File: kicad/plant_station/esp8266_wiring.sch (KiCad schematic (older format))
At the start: 20 parts, among them J1 Conn_02x08_Odd_Even, J17 GPIO, J8 UART, Q4 DMG2301L, U4 ESP-WROOM-02, U5 TPL5110

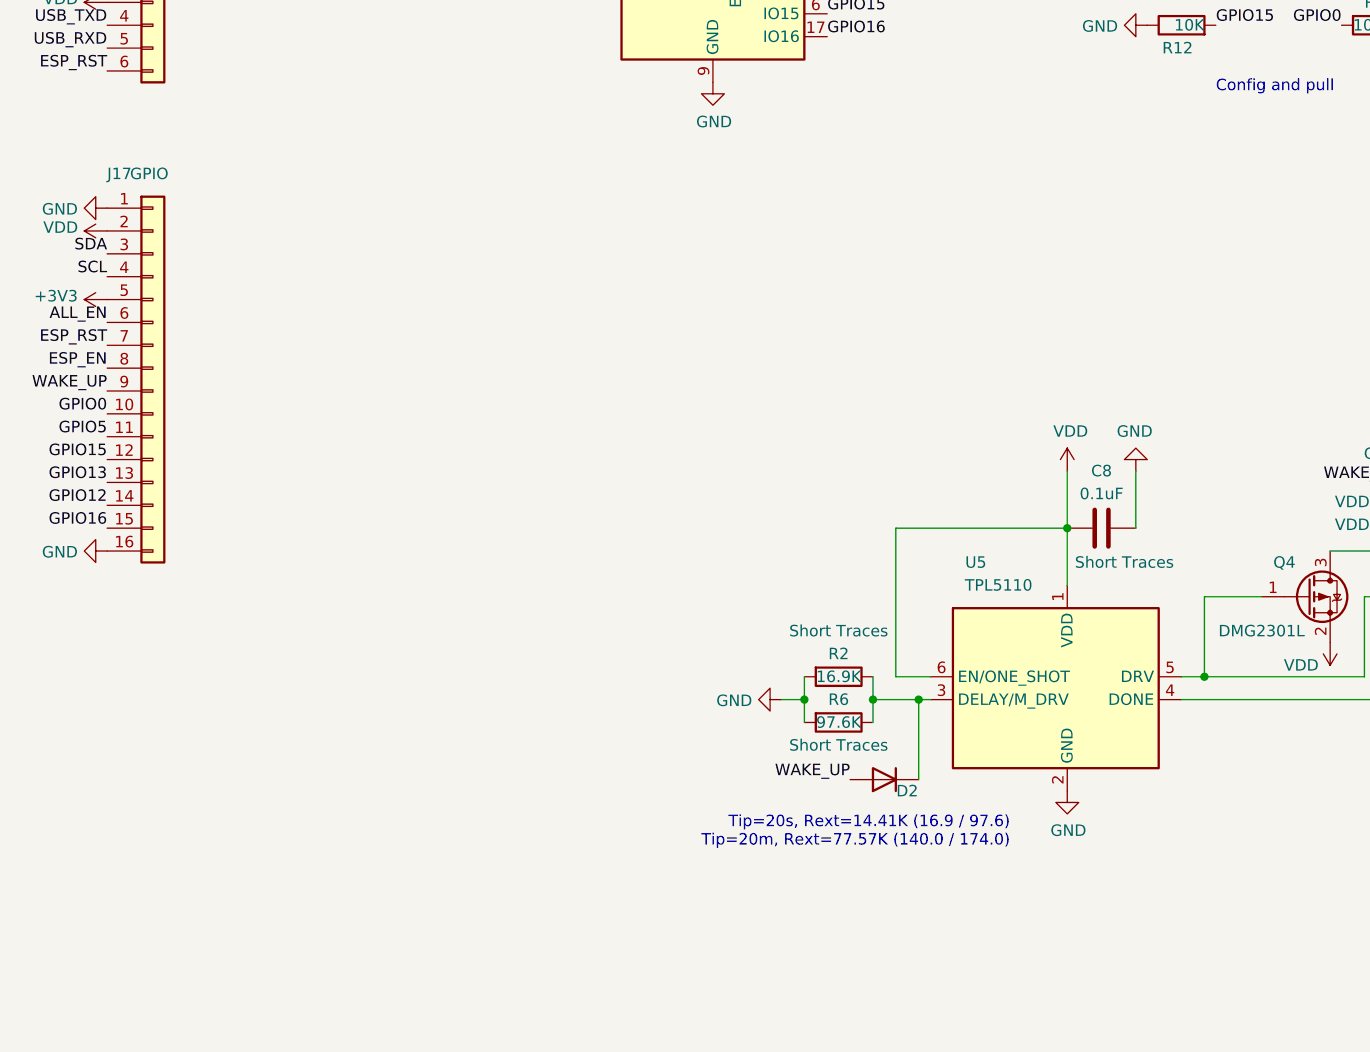
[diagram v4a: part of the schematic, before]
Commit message: Pre-refactoring, diagnostics complete, timer not working properly
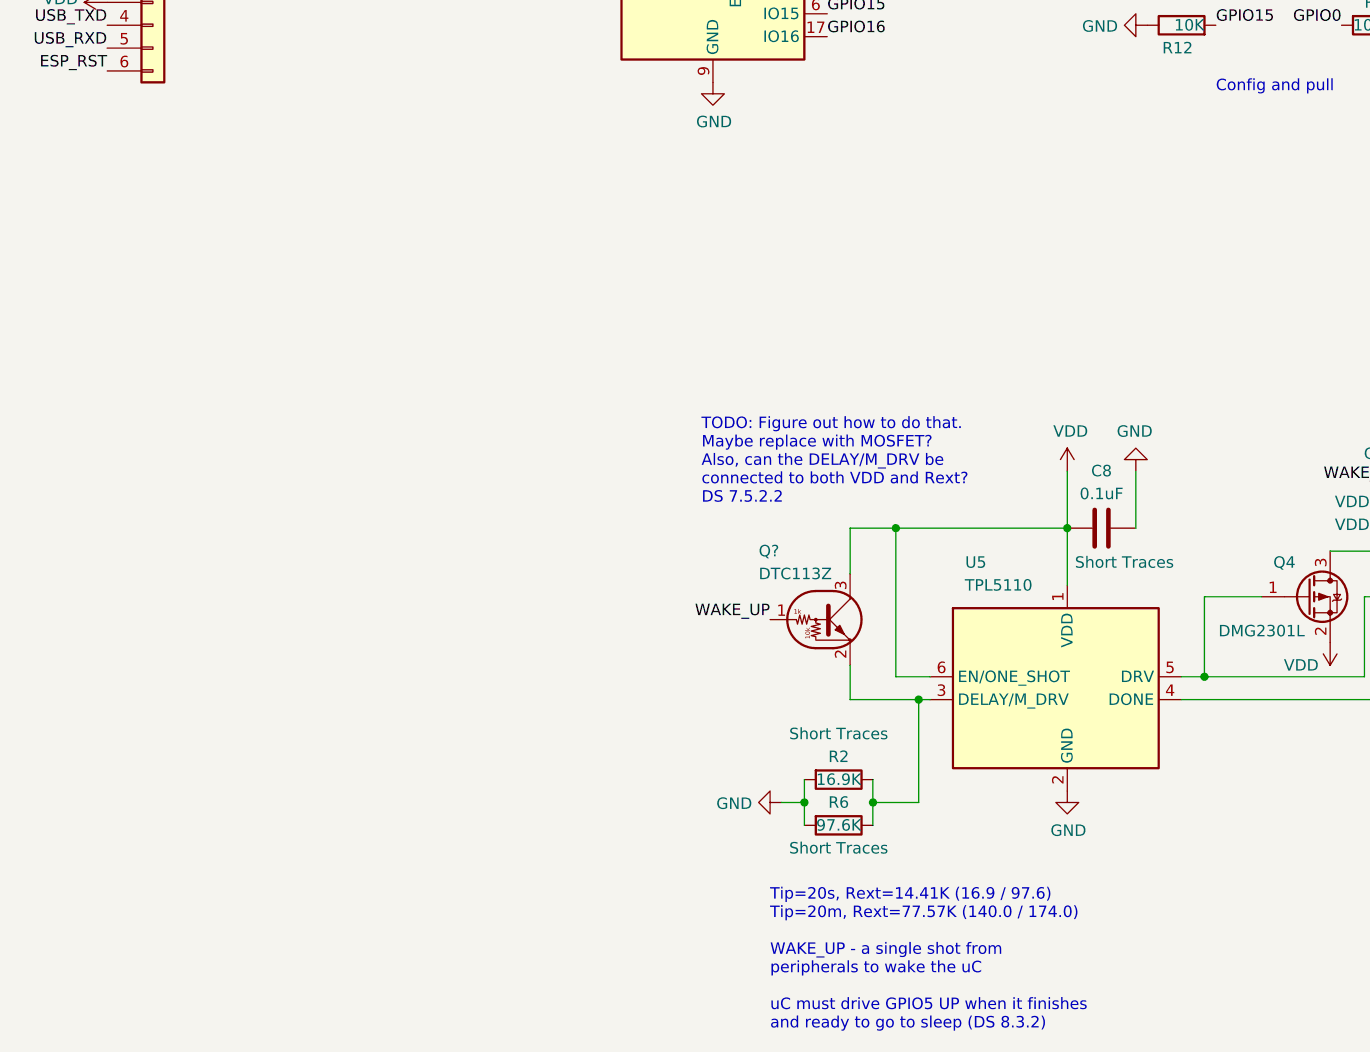
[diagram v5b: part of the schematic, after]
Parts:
- removed D2: LS4148, Parts:MELF_SOD_80_3_BZT55B13GS08, symbol Device:D
- removed J17: GPIO, Connector_PinHeader_2.54mm:PinHeader_1x16_P2.54mm_Vertical, symbol Connector_Generic:Conn_01x16
- added Q?: DTC113Z, symbol Transistor_BJT:DTC113Z
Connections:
- net HOST_WAKE_UP: now also Q?.1 (B)
- net VDD: now also Q?.3 (C)
- net at R2.1, R6.1, U5.3 (DELAY/M_DRV): now also Q?.2 (E)
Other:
- note added: "TODO: Figure out how to do that.\nMaybe replace with MOSFET?\nAlso, can the DELAY/M_DRV be \nconnected to both VDD and Rext? \nDS 7.5.2.2"
- note added: "Tip=20s, Rext=14.41K (16.9 / 97.6)\nTip=20m, Rext=77.57K (140.0 / 174.0)\n\nWAKE_UP - a single shot from \nperipherals to wake the uC\n\nuC must drive GPIO5 UP when it finishes \nand ready to go to sleep (DS 8.3.2)"
- note removed: "Tip=20s, Rext=14.41K (16.9 / 97.6)\nTip=20m, Rext=77.57K (140.0 / 174.0)"
- moved on the sheet: R2, R6
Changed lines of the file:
@@
 	1    0    0    -1
 $EndComp
-Text Label 1900 3900 2    50   ~ 0
-ESP_RST
 $Comp
 L power:GND #PWR049
@@
 L power:GND #PWR031
 U 1 1 5F7FBED9
-P 4850 5450
-F 0 "#PWR031" H 4850 5200 50  0001 C CNN
-F 1 "GND" V 4855 5322 50  0000 R CNN
-F 2 "" H 4850 5450 50  0001 C CNN
-F 3 "" H 4850 5450 50  0001 C CNN
-	1    4850 5450
+P 4850 5900
+F 0 "#PWR031" H 4850 5650 50  0001 C CNN
+F 1 "GND" V 4855 5772 50  0000 R CNN
+F 2 "" H 4850 5900 50  0001 C CNN
+F 3 "" H 4850 5900 50  0001 C CNN
+	1    4850 5900
 	0    1    1    0
 $EndComp
@@
 L Device:R R2
 U 1 1 5F800035
-P 5100 5350
-F 0 "R2" V 5000 5350 50  0000 C CNN
-F 1 "16.9K" V 5100 5350 50  0000 C CNN
-F 2 "Resistor_SMD:R_0805_2012Metric" V 5030 5350 50  0001 C CNN
-F 3 "~" H 5100 5350 50  0001 C CNN
-F 4 "Short Traces" V 4900 5350 50  0000 C CNN "Note"
-	1    5100 5350
-	0    1    1    0
-$EndComp
-Text Label 5150 5800 2    50   ~ 0
+P 5100 5800
+F 0 "R2" V 5000 5800 50  0000 C CNN
+F 1 "16.9K" V 5100 5800 50  0000 C CNN
+F 2 "Resistor_SMD:R_0805_2012Metric" V 5030 5800 50  0001 C CNN
+F 3 "~" H 5100 5800 50  0001 C CNN
+F 4 "Short Traces" V 4900 5800 50  0000 C CNN "Note"
+	1    5100 5800
+	0    1    1    0
+$EndComp
+Text Label 4800 5100 2    50   ~ 0
 WAKE_UP
-$Comp
-L Device:D D2
-U 1 1 5F80D3D3
-P 5300 5800
-F 0 "D2" H 5200 5850 50  0000 C CNN
-F 1 "LS4148" H 5200 5750 50  0001 C CNN
-F 2 "Parts:MELF_SOD_80_3_BZT55B13GS08" H 5300 5800 50  0001 C CNN
-F 3 "~" H 5300 5800 50  0001 C CNN
-	1    5300 5800
-	-1   0    0    1
-$EndComp
-Wire Wire Line
-	5250 5450 5450 5450
-Connection ~ 5450 5450
+Wire Wire Line
+	5250 5900 5450 5900
 Wire Wire Line
 	5450 5450 5500 5450
-Text Notes 5850 6100 2    50   ~ 0
-Tip=20s, Rext=14.41K (16.9 / 97.6)\nTip=20m, Rext=77.57K (140.0 / 174.0)
+Text Notes 4800 6900 0    50   ~ 0
+Tip=20s, Rext=14.41K (16.9 / 97.6)\nTip=20m, Rext=77.57K (140.0 / 174.0)\n\nWAKE_UP - a single shot from \nperipherals to wake the uC\n\nuC must drive GPIO5 UP when it finishes \nand ready to go to sleep (DS 8.3.2)
 $Comp
 L Device:R R6
 U 1 1 5F850A50
-P 5100 5550
-F 0 "R6" V 5000 5550 50  0000 C CNN
-F 1 "97.6K" V 5100 5550 50  0000 C CNN
-F 2 "Resistor_SMD:R_0805_2012Metric" V 5030 5550 50  0001 C CNN
-F 3 "~" H 5100 5550 50  0001 C CNN
-F 4 "Short Traces" V 5200 5550 50  0000 C CNN "Note"
-	1    5100 5550
-	0    1    1    0
-$EndComp
-Wire Wire Line
-	5250 5350 5250 5450
-Connection ~ 5250 5450
-Wire Wire Line
-	5250 5450 5250 5550
-Wire Wire Line
-	5450 5450 5450 5800
+P 5100 6000
+F 0 "R6" V 5000 6000 50  0000 C CNN
+F 1 "97.6K" V 5100 6000 50  0000 C CNN
+F 2 "Resistor_SMD:R_0805_2012Metric" V 5030 6000 50  0001 C CNN
+F 3 "~" H 5100 6000 50  0001 C CNN
+F 4 "Short Traces" V 5200 6000 50  0000 C CNN "Note"
+	1    5100 6000
+	0    1    1    0
+$EndComp
+Wire Wire Line
+	5250 5800 5250 5900
+Connection ~ 5250 5900
+Wire Wire Line
+	5250 5900 5250 6000
 $Comp
 L power:VDD #PWR034
@@
 	5350 4700 5350 5350
 Wire Wire Line
-	4950 5350 4950 5450
-Connection ~ 4950 5450
-Wire Wire Line
-	4950 5450 4950 5550
+	4950 5800 4950 5900
+Connection ~ 4950 5900
+Wire Wire Line
+	4950 5900 4950 6000
 $Comp
 L Timer:TPL5110 U5
@@
 $EndComp
 Wire Wire Line
-	4950 5450 4850 5450
+	4950 5900 4850 5900
 $Comp
 L power:VDD #PWR033
@@
 	0    1    1    0
 $EndComp
-Text Label 1900 4000 2    50   ~ 0
-ESP_EN
-Text Label 1900 4200 2    50   ~ 0
-GPIO0
-Text Label 1900 4300 2    50   ~ 0
-GPIO5
-Text Label 1900 4600 2    50   ~ 0
-GPIO12
-Text Label 1900 4500 2    50   ~ 0
-GPIO13
-Text Label 1900 4400 2    50   ~ 0
-GPIO15
-Text Label 1900 3500 2    50   ~ 0
-SDA
-Text Label 1900 3600 2    50   ~ 0
-SCL
-$Comp
-L power:GND #PWR0101
-U 1 1 5FAF47F5
-P 1900 3300
-F 0 "#PWR0101" H 1900 3050 50  0001 C CNN
-F 1 "GND" V 1905 3172 50  0000 R CNN
-F 2 "" H 1900 3300 50  0001 C CNN
-F 3 "" H 1900 3300 50  0001 C CNN
-	1    1900 3300
-	0    1    1    0
-$EndComp
-$Comp
-L power:VDD #PWR0103
-U 1 1 5FAF61A2
-P 1900 3400
-F 0 "#PWR0103" H 1900 3250 50  0001 C CNN
-F 1 "VDD" V 1915 3527 50  0000 L CNN
-F 2 "" H 1900 3400 50  0001 C CNN
-F 3 "" H 1900 3400 50  0001 C CNN
-	1    1900 3400
-	0    -1   -1   0
-$EndComp
-$Comp
-L Connector_Generic:Conn_01x16 J17
-U 1 1 5F3F86A0
-P 2100 4000
-F 0 "J17" H 1900 4850 50  0000 L CNN
-F 1 "GPIO" H 2000 4850 50  0000 L CNN
-F 2 "Connector_PinHeader_2.54mm:PinHeader_1x16_P2.54mm_Vertical" H 2100 4000 50  0001 C CNN
-F 3 "~" H 2100 4000 50  0001 C CNN
-	1    2100 4000
-	1    0    0    -1
-$EndComp
-Text Label 1900 3800 2    50   ~ 0
-ALL_EN
 Wire Wire Line
 	6700 5350 6600 5350
@@
 	7550 5100 7550 5200
 Connection ~ 7550 5200
-Text Label 1900 4700 2    50   ~ 0
-GPIO16
 Text Label 5050 2550 0    50   ~ 0
 GPIO16
 Text Label 8050 4500 0    50   ~ 0
 GPIO16
-$Comp
-L power:GND #PWR032
-U 1 1 5F51053F
-P 1900 4800
-F 0 "#PWR032" H 1900 4550 50  0001 C CNN
-F 1 "GND" V 1905 4672 50  0000 R CNN
-F 2 "" H 1900 4800 50  0001 C CNN
-F 3 "" H 1900 4800 50  0001 C CNN
-	1    1900 4800
-	0    1    1    0
-$EndComp
 Text Label 9350 3150 2    50   ~ 0
 SDA
@@
 Wire Wire Line
 	8500 4700 8500 4850
-Text Label 1900 4100 2    50   ~ 0
-WAKE_UP
-$Comp
-L power:+3V3 #PWR0104
-U 1 1 5FAF7387
-P 1900 3700
-F 0 "#PWR0104" H 1900 3550 50  0001 C CNN
-F 1 "+3V3" V 1915 3828 50  0000 L CNN
-F 2 "" H 1900 3700 50  0001 C CNN
-F 3 "" H 1900 3700 50  0001 C CNN
-	1    1900 3700
-	0    -1   -1   0
-$EndComp
+Wire Wire Line
+	5450 5450 5450 5900
+Connection ~ 5450 5450
+$Comp
+L Transistor_BJT:DTC113Z Q?
+U 1 1 60F12921
+P 5050 5100
+F 0 "Q?" H 4750 5400 50  0000 L CNN
+F 1 "DTC113Z" H 4750 5300 50  0000 L CNN
+F 2 "" H 5050 5100 50  0001 L CNN
+F 3 "" H 5050 5100 50  0001 L CNN
+	1    5050 5100
+	1    0    0    -1
+$EndComp
+Wire Wire Line
+	5150 5300 5150 5450
+Wire Wire Line
+	5150 5450 5450 5450
+Wire Wire Line
+	5150 4900 5150 4700
+Wire Wire Line
+	5150 4700 5350 4700
+Connection ~ 5350 4700
+Text Notes 4500 4600 0    50   ~ 0
+TODO: Figure out how to do that.\nMaybe replace with MOSFET?\nAlso, can the DELAY/M_DRV be \nconnected to both VDD and Rext? \nDS 7.5.2.2
 $EndSCHEMATC
